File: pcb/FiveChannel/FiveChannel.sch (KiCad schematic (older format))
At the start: 14 parts, among them J101 UPDI, J102 NeoPixel Data, J103 Power Out, J104 5V In, J105 GPIO_A, J106 GPIO_B, J107 GPIO_C, U101 ATTINY1614

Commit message: Filled out the schematic for the five channels
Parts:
- removed J102: NeoPixel Data, Pin_Headers:Pin_Header_Straight_1x02_Pitch2.54mm, symbol Conn_01x02_Male
- removed J103: Power Out, Pin_Headers:Pin_Header_Straight_1x02_Pitch2.54mm, symbol Conn_01x02_Male
- removed R101: 470Ω, Resistors_SMD:R_0805_HandSoldering, symbol R
- added C103: 0.1μF 16V, Capacitors_SMD:C_0805_HandSoldering, symbol C
- gave numbers to parts that had none: 1
- renumbered C102 to C101, C103 to C102, J104 to J102, J107 to J103, J105 to J104, J106 to J105, R102 to R101, U101 to U102
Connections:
- net labels removed: NP_DATA, PA1, PA2, PA3, PA4
- wire segments 77 -> 66
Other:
- note removed: "The NoePixel has JST \nSM type connnectors"
- moved on the sheet: J105

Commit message: Started the layout
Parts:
- removed C101: 1000μF 25V, advent_sternla:CP_Radial_L21.0mm_D13.0mm_P5.00mm_Horizontal, symbol CP
- removed J103: GPIO_C, Pin_Headers:Pin_Header_Straight_1x04_Pitch2.54mm, symbol Conn_01x04_Male
- removed J104: GPIO_A, Pin_Headers:Pin_Header_Straight_1x03_Pitch2.54mm, symbol Conn_01x03_Male
- removed J105: GPIO_B, Pin_Headers:Pin_Header_Straight_1x04_Pitch2.54mm, symbol Conn_01x04_Male
- U101: footprint (none) -> Housings_SOIC:SOIC-16_3.9x9.9mm_Pitch1.27mm; ConradPN (none) -> Value; Label (none) -> Value; MPN (none) -> Value
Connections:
- net labels removed: PA5, PA6, PA7, PB0, PB1, PB2, PB3
- wire segments 66 -> 44
- no-connect marks 8 -> 15
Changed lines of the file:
@@
 Text Label 7150 4300 2    60   ~ 0
 ~ENABLE
-Text Label 7150 4450 2    60   ~ 0
-PA5
-Text Label 7150 4600 2    60   ~ 0
-PA6
-Text Label 7150 4750 2    60   ~ 0
-PA7
-$Comp
-L Conn_01x03_Male J104
-U 1 1 59EF8E2B
-P 8400 5450
-F 0 "J104" H 8350 5650 50  0000 C CNN
-F 1 "GPIO_A" H 8550 5300 50  0000 C CNN
-F 2 "Pin_Headers:Pin_Header_Straight_1x03_Pitch2.54mm" H 8400 5450 50  0001 C CNN
-F 3 "" H 8400 5450 50  0001 C CNN
-	1    8400 5450
-	-1   0    0    -1
-$EndComp
-$Comp
-L Conn_01x04_Male J103
-U 1 1 59EF90A2
-P 3600 4750
-F 0 "J103" H 3600 4950 50  0000 C CNN
-F 1 "GPIO_C" H 3600 4450 50  0000 C CNN
-F 2 "Pin_Headers:Pin_Header_Straight_1x04_Pitch2.54mm" H 3600 4750 50  0001 C CNN
-F 3 "" H 3600 4750 50  0001 C CNN
-	1    3600 4750
-	1    0    0    -1
-$EndComp
-Text Label 4250 4500 0    60   ~ 0
-PB0
-Text Label 4250 4650 0    60   ~ 0
-PB1
-Text Label 4250 4800 0    60   ~ 0
-PB2
-Text Label 4250 4950 0    60   ~ 0
-PB3
 $Comp
 L C C102
@@
 Text Label 2100 3850 0    60   ~ 0
 5V
-$Comp
-L CP C101
-U 1 1 59F0F869
-P 1900 4150
-F 0 "C101" H 1925 4250 50  0000 L CNN
-F 1 "1000μF 25V" H 1925 4050 50  0000 L CNN
-F 2 "advent_sternla:CP_Radial_L21.0mm_D13.0mm_P5.00mm_Horizontal" H 1938 4000 50  0001 C CNN
-F 3 "" H 1900 4150 50  0001 C CNN
-	1    1900 4150
-	1    0    0    -1
-$EndComp
 Wire Wire Line
 	3800 4300 4800 4300
@@
 	2000 1350 2450 1350
 Wire Wire Line
-	6450 4450 7150 4450
-Wire Wire Line
-	6450 4600 7150 4600
-Wire Wire Line
-	6450 4750 7150 4750
-Wire Wire Line
 	1300 3850 2500 3850
 Wire Wire Line
-	4100 4650 4800 4650
-Wire Wire Line
-	4800 4950 3800 4950
-Wire Wire Line
 	3250 3850 3250 4050
 Wire Wire Line
@@
 	700  2100 700  900
 Wire Wire Line
-	4150 4800 4800 4800
-Wire Wire Line
-	4150 4800 4150 4850
-Wire Wire Line
-	4150 4850 3800 4850
-Wire Wire Line
-	4100 4650 4100 4750
-Wire Wire Line
-	4100 4750 3800 4750
-Wire Wire Line
-	4800 4500 4050 4500
-Wire Wire Line
-	4050 4500 4050 4650
-Wire Wire Line
-	4050 4650 3800 4650
-Wire Wire Line
-	1900 3850 1900 4000
-Connection ~ 1900 3850
-Wire Wire Line
-	1900 4300 1900 4700
-Wire Wire Line
 	1500 4700 3250 4700
 Wire Wire Line
 	2550 4700 2550 4900
-Connection ~ 1900 4700
 Connection ~ 2550 4700
 $Comp
@@
 F 0 "U101" H 9450 4700 70  0000 C CNN
 F 1 "74LS596" H 9300 3500 70  0000 C CNN
-F 2 "" H 9300 4100 60  0001 C CNN
+F 2 "Housings_SOIC:SOIC-16_3.9x9.9mm_Pitch1.27mm" H 9300 4100 60  0001 C CNN
 F 3 "" H 9300 4100 60  0000 C CNN
+F 4 "Value" H 9300 4100 60  0001 C CNN "MPN"
+F 5 "Value" H 9300 4100 60  0001 C CNN "ConradPN"
+F 6 "Value" H 9300 4100 60  0000 C CNN "Label"
 	1    9300 4100
 	1    0    0    -1
@@
 Wire Wire Line
 	9000 4950 9000 5100
-Wire Wire Line
-	8200 6000 7500 6000
-Wire Wire Line
-	8200 6100 7500 6100
-Wire Wire Line
-	8200 6200 7500 6200
-Text Label 7500 6000 0    60   ~ 0
-PA5
-Text Label 7500 6100 0    60   ~ 0
-PA6
-Text Label 7500 6200 0    60   ~ 0
-PA7
 Text Label 7750 3650 0    60   ~ 0
 DATA_PIN
@@
 CHANNEL_4
 Wire Wire Line
-	8200 5900 7500 5900
-$Comp
-L Conn_01x04_Male J105
-U 1 1 59EF8DC0
-P 8400 6000
-F 0 "J105" H 8400 6200 50  0000 C CNN
-F 1 "GPIO_B" H 8500 5750 50  0000 C CNN
-F 2 "Pin_Headers:Pin_Header_Straight_1x04_Pitch2.54mm" H 8400 6000 50  0001 C CNN
-F 3 "" H 8400 6000 50  0001 C CNN
-	1    8400 6000
-	-1   0    0    -1
-$EndComp
-Wire Wire Line
-	8200 5550 7500 5550
-Wire Wire Line
-	8200 5450 7500 5450
-Wire Wire Line
-	8200 5350 7500 5350
-Wire Wire Line
 	9300 3250 9300 3050
 Wire Wire Line
@@
 Text Label 8850 3050 0    60   ~ 0
 VDD
-Text Label 7500 5350 0    60   ~ 0
-DATA_PIN
-Text Label 7500 5450 0    60   ~ 0
-CLK_PIN
-Text Label 7500 5550 0    60   ~ 0
-LATCH_PIN
-Text Label 7500 5900 0    60   ~ 0
-~ENABLE
 $Sheet
 S 5250 1100 1100 1750
@@
 Wire Wire Line
 	7950 4900 7950 4750
+NoConn ~ 4800 4500
+NoConn ~ 4800 4650
+NoConn ~ 4800 4800
+NoConn ~ 4800 4950
+NoConn ~ 6450 4450
+NoConn ~ 6450 4600
+NoConn ~ 6450 4750
 $EndSCHEMATC

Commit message: Working through the five channel prototype layout
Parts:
- added C101: 1000μF 25V, advent_sternla:CP_Radial_L21.0mm_D13.0mm_P5.00mm_Horizontal, symbol C
- added J103: Conn_01x04_Male, Pin_Headers:Pin_Header_Angled_1x04_Pitch2.54mm, symbol Conn_01x04_Male
- added J104: Conn_01x07_Male, Pin_Headers:Pin_Header_Angled_1x07_Pitch2.54mm, symbol Conn_01x07_Male
- U101: symbol 74LS596 -> 74LS596-RESCUE-FiveChannel
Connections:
- net 5V: now also C101.1
- net CLK_PIN: now also J104.2 (Pin_2)
- net DATA_PIN: now also J104.1 (Pin_1)
- net GND: now also C101.2
- net LATCH_PIN: now also J104.3 (Pin_3)
- net ~ENABLE: now also J104.4 (Pin_4)
- net PA5: now reaches U102.3 (PA5)
- net PA5: now also J104.5 (Pin_5)
- net PA6: now reaches U102.4 (PA6)
- net PA6: now also J104.6 (Pin_6)
- net PA7: now reaches U102.5 (PA7)
- net PA7: now also J104.7 (Pin_7)
- net PB3: now reaches U102.6 (TOSC1/PB3)
- net PB3: now also J103.4 (Pin_4)
- net PB2: now reaches U102.7 (TOSC2/PB2)
- net PB2: now also J103.3 (Pin_3)
- net PB1: now reaches U102.8 (PB1)
- net PB1: now also J103.2 (Pin_2)
- net PB0: now reaches U102.9 (PB0)
- net PB0: now also J103.1 (Pin_1)
- no-connect marks 15 -> 8
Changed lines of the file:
@@
 EESchema Schematic File Version 2
+LIBS:FiveChannel-rescue
 LIBS:advent_sternla_attiny1614_symbols
 LIBS:SensorBoard
@@
 VDD
 $Comp
-L GND #PWR01
+L GND #PWR105
 U 1 1 59EF6C0B
 P 5600 5550
-F 0 "#PWR01" H 5600 5300 50  0001 C CNN
+F 0 "#PWR105" H 5600 5300 50  0001 C CNN
 F 1 "GND" H 5600 5400 50  0000 C CNN
 F 2 "" H 5600 5550 50  0001 C CNN
@@
 PDI_DATA
 $Comp
-L GND #PWR02
+L GND #PWR101
 U 1 1 59EF6D08
 P 2250 1750
-F 0 "#PWR02" H 2250 1500 50  0001 C CNN
+F 0 "#PWR101" H 2250 1500 50  0001 C CNN
 F 1 "GND" H 2250 1600 50  0000 C CNN
 F 2 "" H 2250 1750 50  0001 C CNN
@@
 VDD
 $Comp
-L GND #PWR03
+L GND #PWR102
 U 1 1 59EF8502
 P 2550 4900
-F 0 "#PWR03" H 2550 4650 50  0001 C CNN
+F 0 "#PWR102" H 2550 4650 50  0001 C CNN
 F 1 "GND" H 2550 4750 50  0000 C CNN
 F 2 "" H 2550 4900 50  0001 C CNN
@@
 Text Label 2100 3850 0    60   ~ 0
 5V
-Wire Wire Line
-	3800 4300 4800 4300
-Wire Wire Line
-	4600 4300 4600 4200
-Wire Wire Line
-	5600 5550 5600 5250
-Connection ~ 4600 4300
-Wire Wire Line
-	1500 1350 1050 1350
-Wire Wire Line
-	2000 1550 2250 1550
-Wire Wire Line
-	2250 1550 2250 1750
-Wire Wire Line
-	2000 1350 2450 1350
-Wire Wire Line
-	1300 3850 2500 3850
-Wire Wire Line
-	3250 3850 3250 4050
-Wire Wire Line
-	3250 4700 3250 4350
-Wire Notes Line
-	700  900  3000 900
-Wire Notes Line
-	3000 900  3000 2100
-Wire Notes Line
-	3000 2100 700  2100
-Wire Notes Line
-	700  2100 700  900
-Wire Wire Line
-	1500 4700 3250 4700
-Wire Wire Line
-	2550 4700 2550 4900
-Connection ~ 2550 4700
 $Comp
 L Jack-DC J102
@@
 	1    0    0    -1
 $EndComp
-Wire Wire Line
-	1500 4700 1500 4050
-Wire Wire Line
-	1500 4050 1300 4050
 NoConn ~ 1300 3950
-Wire Wire Line
-	2000 3850 2000 3500
-Wire Wire Line
-	2000 3500 2250 3500
-Connection ~ 2000 3850
 Text Label 2250 3500 2    60   ~ 0
 5V_OUT
@@
 	-1   0    0    1
 $EndComp
-Wire Wire Line
-	2800 3850 4800 3850
-Connection ~ 3250 3850
-Wire Wire Line
-	4600 3900 4600 3850
-Connection ~ 4600 3850
 Text Notes 1550 6150 0    60   ~ 0
 TODO \nVerify, once more, the Diode i.e. the current rating\nDouble check the connection for the UPDI - is there a need for a \nzero Ohm resistor to deal with any issues?
 $Comp
-L 74LS596 U101
+L 74LS596-RESCUE-FiveChannel U101
 U 1 1 5A60F031
 P 9300 4100
@@
 	1    0    0    -1
 $EndComp
-Wire Wire Line
-	6650 3850 6650 3650
-Wire Wire Line
-	6650 3650 8600 3650
-Wire Wire Line
-	10000 3650 10600 3650
-Wire Wire Line
-	10000 3750 10600 3750
-Wire Wire Line
-	10000 3850 10600 3850
-Wire Wire Line
-	10000 3950 10600 3950
-Wire Wire Line
-	10000 4050 10600 4050
 NoConn ~ 10000 4150
 NoConn ~ 10000 4250
@@
 NoConn ~ 10000 4550
 $Comp
-L GND #PWR04
+L GND #PWR104
 U 1 1 5A60F656
 P 9000 5100
-F 0 "#PWR04" H 9000 4850 50  0001 C CNN
+F 0 "#PWR104" H 9000 4850 50  0001 C CNN
 F 1 "GND" H 9000 4950 50  0000 C CNN
 F 2 "" H 9000 5100 50  0001 C CNN
@@
 	1    0    0    -1
 $EndComp
-Wire Wire Line
-	9000 4950 9000 5100
 Text Label 7750 3650 0    60   ~ 0
 DATA_PIN
-Wire Wire Line
-	6450 3850 6650 3850
-Wire Wire Line
-	6450 4000 6700 4000
-Wire Wire Line
-	6700 4000 6700 3850
 Text Label 8200 3950 0    60   ~ 0
 VDD
-Wire Wire Line
-	6700 3850 8600 3850
-Wire Wire Line
-	8200 3950 8600 3950
-Wire Wire Line
-	6450 4150 8600 4150
-Wire Wire Line
-	6450 4300 7150 4300
 Text Label 10600 3650 2    60   ~ 0
 CHANNEL_0
@@
 Text Label 10600 4050 2    60   ~ 0
 CHANNEL_4
-Wire Wire Line
-	9300 3250 9300 3050
-Wire Wire Line
-	9300 3050 8850 3050
 Text Label 8850 3050 0    60   ~ 0
 VDD
@@
 F7 "CHANNEL_4" I L 5250 2500 60
 $EndSheet
-Wire Wire Line
-	5250 1450 4650 1450
-Wire Wire Line
-	5250 1700 4650 1700
-Wire Wire Line
-	5250 1950 4650 1950
-Wire Wire Line
-	5250 2250 4650 2250
-Wire Wire Line
-	5250 2500 4650 2500
-Text Label 4650 2750 0    60   ~ 0
-VDD
 Text Label 4650 2500 0    60   ~ 0
 CHANNEL_4
@@
 Text Label 4650 1950 0    60   ~ 0
 CHANNEL_2
-Wire Wire Line
-	5250 2750 4650 2750
-Wire Wire Line
-	8600 4250 8150 4250
 Text Label 8150 4250 0    60   ~ 0
 ~ENABLE
-Wire Wire Line
-	7950 4150 7950 4450
-Connection ~ 7950 4150
 $Comp
 L C C103
@@
 $EndComp
 $Comp
-L GND #PWR05
+L GND #PWR103
 U 1 1 5A61342B
 P 7950 4900
-F 0 "#PWR05" H 7950 4650 50  0001 C CNN
+F 0 "#PWR103" H 7950 4650 50  0001 C CNN
 F 1 "GND" H 7950 4750 50  0000 C CNN
 F 2 "" H 7950 4900 50  0001 C CNN
@@
 	1    0    0    -1
 $EndComp
+$Comp
+L Conn_01x04_Male J103
+U 1 1 5A64D382
+P 6750 5650
+F 0 "J103" H 6750 5850 50  0000 C CNN
+F 1 "Conn_01x04_Male" H 6750 5350 50  0000 C CNN
+F 2 "Pin_Headers:Pin_Header_Angled_1x04_Pitch2.54mm" H 6750 5650 50  0001 C CNN
+F 3 "" H 6750 5650 50  0001 C CNN
+	1    6750 5650
+	-1   0    0    -1
+$EndComp
+$Comp
+L Conn_01x07_Male J104
+U 1 1 5A64D42F
+P 8100 5800
+F 0 "J104" H 8100 6200 50  0000 C CNN
+F 1 "Conn_01x07_Male" H 8100 5400 50  0000 C CNN
+F 2 "Pin_Headers:Pin_Header_Angled_1x07_Pitch2.54mm" H 8100 5800 50  0001 C CNN
+F 3 "" H 8100 5800 50  0001 C CNN
+	1    8100 5800
+	-1   0    0    -1
+$EndComp
+Wire Wire Line
+	3800 4300 4800 4300
+Wire Wire Line
+	4600 4300 4600 4200
+Wire Wire Line
+	5600 5550 5600 5250
+Connection ~ 4600 4300
+Wire Wire Line
+	1500 1350 1050 1350
+Wire Wire Line
+	2000 1550 2250 1550
+Wire Wire Line
+	2250 1550 2250 1750
+Wire Wire Line
+	2000 1350 2450 1350
+Wire Wire Line
+	1300 3850 2500 3850
+Wire Wire Line
+	3250 3850 3250 4050
+Wire Wire Line
+	3250 4700 3250 4350
+Wire Notes Line
+	700  900  3000 900
+Wire Notes Line
+	3000 900  3000 2100
+Wire Notes Line
+	3000 2100 700  2100
+Wire Notes Line
+	700  2100 700  900
+Wire Wire Line
+	1500 4700 3250 4700
+Wire Wire Line
+	2550 4700 2550 4900
+Connection ~ 2550 4700
+Wire Wire Line
+	1500 4700 1500 4050
+Wire Wire Line
+	1500 4050 1300 4050
+Wire Wire Line
+	2000 3850 2000 3500
+Wire Wire Line
+	2000 3500 2250 3500
+Connection ~ 2000 3850
+Wire Wire Line
+	2800 3850 4800 3850
+Connection ~ 3250 3850
+Wire Wire Line
+	4600 3900 4600 3850
+Connection ~ 4600 3850
+Wire Wire Line
+	6650 3850 6650 3650
+Wire Wire Line
+	6650 3650 8600 3650
+Wire Wire Line
+	10000 3650 10600 3650
+Wire Wire Line
+	10000 3750 10600 3750
+Wire Wire Line
+	10000 3850 10600 3850
+Wire Wire Line
+	10000 3950 10600 3950
+Wire Wire Line
+	10000 4050 10600 4050
+Wire Wire Line
+	9000 4950 9000 5100
+Wire Wire Line
+	6450 3850 6650 3850
+Wire Wire Line
+	6450 4000 6700 4000
+Wire Wire Line
+	6700 4000 6700 3850
+Wire Wire Line
+	6700 3850 8600 3850
+Wire Wire Line
+	8200 3950 8600 3950
+Wire Wire Line
+	6450 4150 8600 4150
+Wire Wire Line
+	6450 4300 7150 4300
+Wire Wire Line
+	9300 3250 9300 3050
+Wire Wire Line
+	9300 3050 8850 3050
+Wire Wire Line
+	5250 1450 4650 1450
+Wire Wire Line
+	5250 1700 4650 1700
+Wire Wire Line
+	5250 1950 4650 1950
+Wire Wire Line
+	5250 2250 4650 2250
+Wire Wire Line
+	5250 2500 4650 2500
+Wire Wire Line
+	5250 2750 4650 2750
+Wire Wire Line
+	8600 4250 8150 4250
+Wire Wire Line
+	7950 4150 7950 4450
+Connection ~ 7950 4150
 Wire Wire Line
 	7950 4900 7950 4750
-NoConn ~ 4800 4500
-NoConn ~ 4800 4650
-NoConn ~ 4800 4800
-NoConn ~ 4800 4950
-NoConn ~ 6450 4450
-NoConn ~ 6450 4600
-NoConn ~ 6450 4750
+Wire Wire Line
+	4800 4500 4100 4500
+Wire Wire Line
+	4800 4650 4100 4650
+Wire Wire Line
+	4800 4800 4100 4800
+Wire Wire Line
+	4800 4950 4100 4950
+Wire Wire Line
+	6550 5550 6150 5550
+Wire Wire Line
+	6550 5650 6150 5650
+Wire Wire Line
+	6550 5750 6150 5750
+Wire Wire Line
+	6550 5850 6150 5850
+Wire Wire Line
+	7900 5500 7300 5500
+Wire Wire Line
+	7900 5600 7300 5600
+Wire Wire Line
+	7900 5700 7300 5700
+Wire Wire Line
+	7900 5800 7300 5800
+Wire Wire Line
+	7900 5900 7300 5900
+Wire Wire Line
+	7900 6000 7300 6000
+Wire Wire Line
+	7900 6100 7300 6100
+Text Label 4100 4500 0    60   ~ 0
+PB0
+Text Label 6150 5550 0    60   ~ 0
+PB0
+Text Label 4100 4650 0    60   ~ 0
+PB1
+Text Label 6150 5650 0    60   ~ 0
+PB1
+Text Label 4100 4800 0    60   ~ 0
+PB2
+Text Label 4100 4950 0    60   ~ 0
+PB3
+Text Label 6150 5750 0    60   ~ 0
+PB2
+Text Label 6150 5850 0    60   ~ 0
+PB3
+Text Label 7300 5900 0    60   ~ 0
+PA5
+Text Label 7300 6000 0    60   ~ 0
+PA6
+Text Label 7300 6100 0    60   ~ 0
+PA7
+Wire Wire Line
+	6450 4450 7150 4450
+Wire Wire Line
+	6450 4600 7150 4600
+Wire Wire Line
+	6450 4750 7150 4750
+Text Label 7150 4750 2    60   ~ 0
+PA7
+Text Label 7150 4600 2    60   ~ 0
+PA6
+Text Label 7150 4450 2    60   ~ 0
+PA5
+Text Label 7300 5800 0    60   ~ 0
+~ENABLE
+Text Label 7000 5100 0    60   ~ 0
+LATCH_PIN
+Text Label 7300 5700 0    60   ~ 0
+LATCH_PIN
+Text Label 7300 5600 0    60   ~ 0
+CLK_PIN
+Text Label 7300 5500 0    60   ~ 0
+DATA_PIN
+$Comp
+L C C101
+U 1 1 5A64D305
+P 1850 4200
+F 0 "C101" H 1875 4300 50  0000 L CNN
+F 1 "1000μF 25V" H 1700 4100 50  0000 L CNN
+F 2 "advent_sternla:CP_Radial_L21.0mm_D13.0mm_P5.00mm_Horizontal" H 1888 4050 50  0001 C CNN
+F 3 "" H 1850 4200 50  0001 C CNN
+F 4 "Value" H 1850 4200 60  0001 C CNN "Link"
+F 5 "Value" H 1850 4200 60  0000 C CNN "Comp_Name"
+	1    1850 4200
+	1    0    0    -1
+$EndComp
+Wire Wire Line
+	1850 3850 1850 4050
+Connection ~ 1850 3850
+Wire Wire Line
+	1850 4350 1850 4700
+Connection ~ 1850 4700
+Text Label 4650 2750 0    60   ~ 0
+5V_OUT
 $EndSCHEMATC

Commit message: Finished the layout and sent to OSH Park
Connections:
- net DATA_PIN: now also J104.3 (Pin_3); no longer J104.1 (Pin_1)
- net LATCH_PIN: now also J104.1 (Pin_1); no longer J104.3 (Pin_3)
- net PB0: now also J103.2 (Pin_2); no longer J103.1 (Pin_1)
- net PB1: now also J103.1 (Pin_1); no longer J103.2 (Pin_2)
- net PB2: now also J103.4 (Pin_4); no longer J103.3 (Pin_3)
- net PB3: now also J103.3 (Pin_3); no longer J103.4 (Pin_4)
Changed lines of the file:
@@
 VDD
 $Comp
-L GND #PWR105
+L GND #PWR01
 U 1 1 59EF6C0B
 P 5600 5550
-F 0 "#PWR105" H 5600 5300 50  0001 C CNN
+F 0 "#PWR01" H 5600 5300 50  0001 C CNN
 F 1 "GND" H 5600 5400 50  0000 C CNN
 F 2 "" H 5600 5550 50  0001 C CNN
@@
 PDI_DATA
 $Comp
-L GND #PWR101
+L GND #PWR02
 U 1 1 59EF6D08
 P 2250 1750
-F 0 "#PWR101" H 2250 1500 50  0001 C CNN
+F 0 "#PWR02" H 2250 1500 50  0001 C CNN
 F 1 "GND" H 2250 1600 50  0000 C CNN
 F 2 "" H 2250 1750 50  0001 C CNN
@@
 VDD
 $Comp
-L GND #PWR102
+L GND #PWR03
 U 1 1 59EF8502
 P 2550 4900
-F 0 "#PWR102" H 2550 4650 50  0001 C CNN
+F 0 "#PWR03" H 2550 4650 50  0001 C CNN
 F 1 "GND" H 2550 4750 50  0000 C CNN
 F 2 "" H 2550 4900 50  0001 C CNN
@@
 NoConn ~ 10000 4550
 $Comp
-L GND #PWR104
+L GND #PWR04
 U 1 1 5A60F656
 P 9000 5100
-F 0 "#PWR104" H 9000 4850 50  0001 C CNN
+F 0 "#PWR04" H 9000 4850 50  0001 C CNN
 F 1 "GND" H 9000 4950 50  0000 C CNN
 F 2 "" H 9000 5100 50  0001 C CNN
@@
 $EndComp
 $Comp
-L GND #PWR103
+L GND #PWR05
 U 1 1 5A61342B
 P 7950 4900
-F 0 "#PWR103" H 7950 4650 50  0001 C CNN
+F 0 "#PWR05" H 7950 4650 50  0001 C CNN
 F 1 "GND" H 7950 4750 50  0000 C CNN
 F 2 "" H 7950 4900 50  0001 C CNN
@@
 Text Label 4100 4500 0    60   ~ 0
 PB0
-Text Label 6150 5550 0    60   ~ 0
+Text Label 6150 5650 0    60   ~ 0
 PB0
 Text Label 4100 4650 0    60   ~ 0
 PB1
-Text Label 6150 5650 0    60   ~ 0
+Text Label 6150 5550 0    60   ~ 0
 PB1
 Text Label 4100 4800 0    60   ~ 0
@@
 Text Label 4100 4950 0    60   ~ 0
 PB3
+Text Label 6150 5850 0    60   ~ 0
+PB2
 Text Label 6150 5750 0    60   ~ 0
-PB2
-Text Label 6150 5850 0    60   ~ 0
 PB3
 Text Label 7300 5900 0    60   ~ 0
@@
 Text Label 7000 5100 0    60   ~ 0
 LATCH_PIN
-Text Label 7300 5700 0    60   ~ 0
+Text Label 7300 5500 0    60   ~ 0
 LATCH_PIN
 Text Label 7300 5600 0    60   ~ 0
 CLK_PIN
-Text Label 7300 5500 0    60   ~ 0
+Text Label 7300 5700 0    60   ~ 0
 DATA_PIN
 $Comp

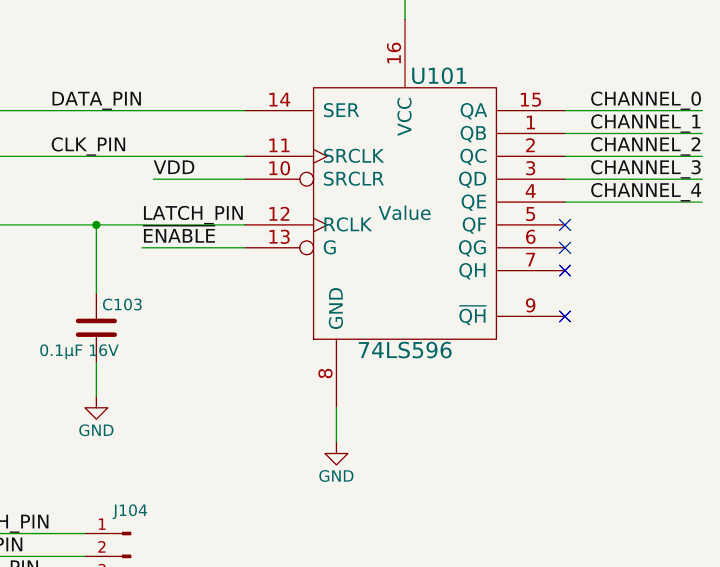
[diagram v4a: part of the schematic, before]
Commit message: All five channels are working
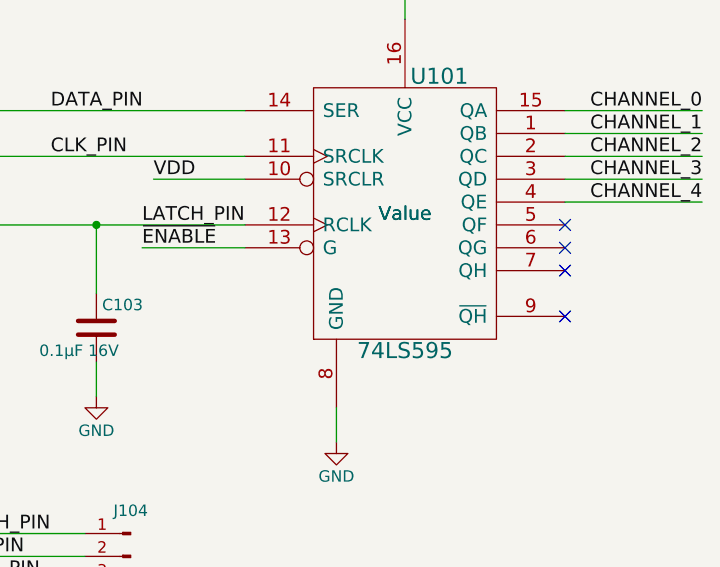
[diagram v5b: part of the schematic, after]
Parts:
- U101: value 74LS596 -> 74LS595; Comp_Name (none) -> Value; Link (none) -> Value
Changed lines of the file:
@@
 LIBS:contrib
 LIBS:valves
-LIBS:FiveChannel-cache
 EELAYER 25 0
 EELAYER END
@@
 P 9300 4100
 F 0 "U101" H 9450 4700 70  0000 C CNN
-F 1 "74LS596" H 9300 3500 70  0000 C CNN
+F 1 "74LS595" H 9300 3500 70  0000 C CNN
 F 2 "Housings_SOIC:SOIC-16_3.9x9.9mm_Pitch1.27mm" H 9300 4100 60  0001 C CNN
 F 3 "" H 9300 4100 60  0000 C CNN
 F 4 "Value" H 9300 4100 60  0001 C CNN "MPN"
-F 5 "Value" H 9300 4100 60  0001 C CNN "ConradPN"
-F 6 "Value" H 9300 4100 60  0000 C CNN "Label"
+F 5 "Value" H 9300 4100 60  0001 C CNN "Link"
+F 6 "Value" H 9300 4100 60  0000 C CNN "Comp_Name"
+F 7 "Value" H 9300 4100 60  0001 C CNN "ConradPN"
+F 8 "Value" H 9300 4100 60  0000 C CNN "Label"
 	1    9300 4100
 	1    0    0    -1
